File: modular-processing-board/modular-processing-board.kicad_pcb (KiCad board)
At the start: 6 copper layers, 90 x 90 mm, 175 parts, among them J1001 BWU.FL-IPEX1, J202 Conn_02x06_Odd_Even, J401 TF01A, J501 Plug_Hirose_DF40_2x40_DF40C-8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, J502 Conn_02x06_Odd_Even, J601 Conn_Coaxial_Small, J602 BWU.FL-IPEX1, J604 Conn_Coaxial_Small, J701 Conn_02x02_Odd_Even, J801 TYPE-C-31-M-12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

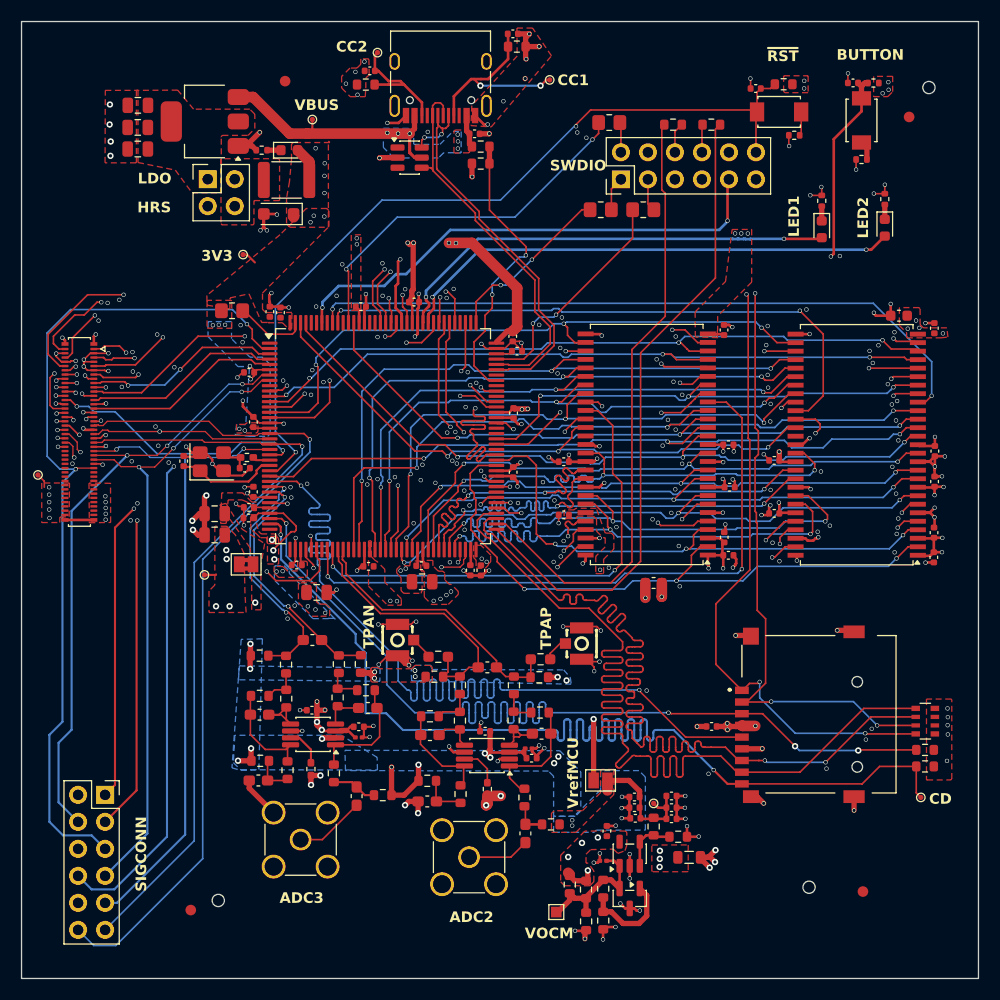
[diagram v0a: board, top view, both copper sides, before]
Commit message: checked components part numbers (next) board checks
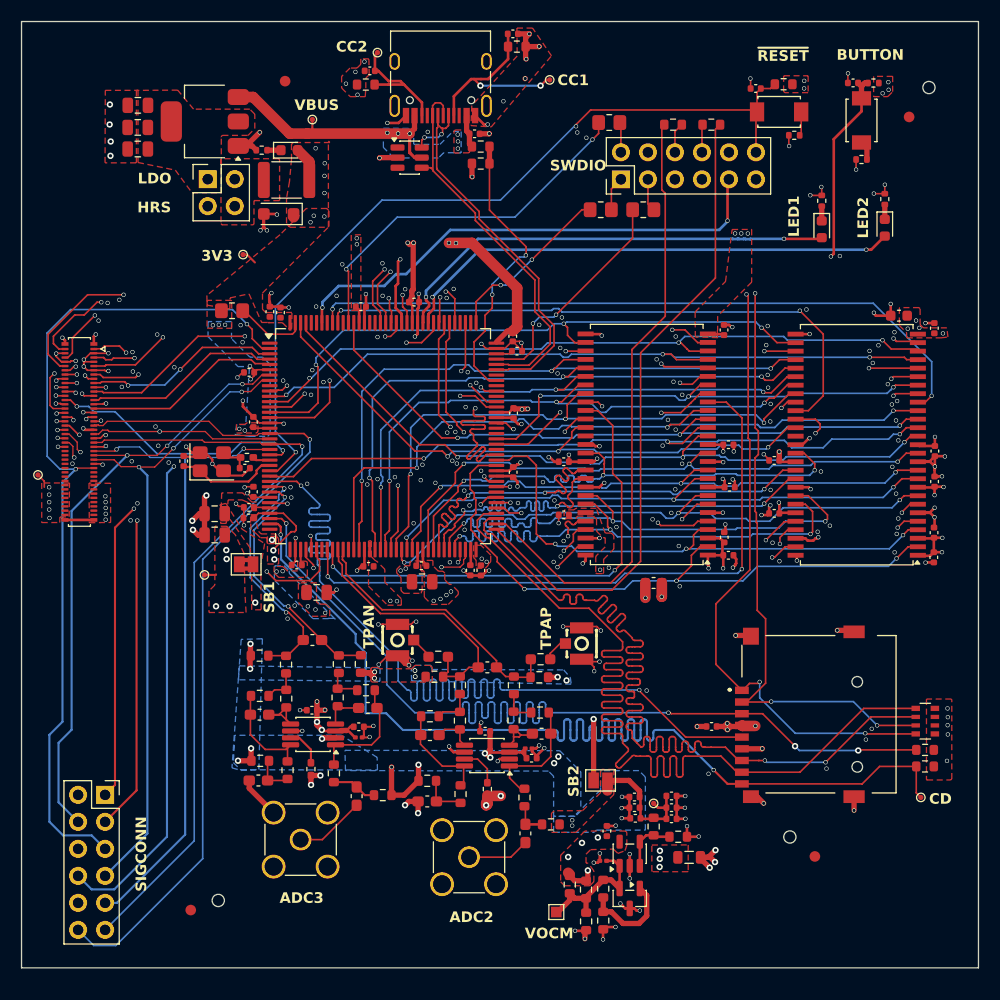
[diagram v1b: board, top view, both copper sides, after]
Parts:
- moved FID101 5.60 mm to (122.6, 126.5)
- moved H101 5.06 mm to (120.3, 124.7)
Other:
- board size 90 x 90 mm -> 90 x 89 mm
- board text added: "SB1"
- board text added: "SB2"
- board text added: "~{RESET}"
- board text removed: "VrefMCU"
- board text removed: "~{RST}"
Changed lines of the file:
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@@
 	(footprint "MountingHole:ToolingHole_1.152mm"
 		(layer "F.Cu")
-		(at 122.066 129.4178 90)
+		(at 120.2626 124.6934 90)
 		(descr "Tooling Hole 1.152mm, 1.3mm solder mask, JLCPCB specification, https://jlcpcb.com/help/article/How-to-add-tooling-holes-for-PCB-assembly-order")
 		(tags "mounting")
@@
 			(polygon
 				(pts
-					(xy 122.066 128.7178) (xy 121.898479 128.738141) (xy 121.740694 128.797981) (xy 121.601814 128.893842)
-					(xy 121.489911 129.020155) (xy 121.411489 129.169577) (xy 121.371104 129.333424) (xy 121.371104 129.502176)
-					(xy 121.411489 129.666023) (xy 121.489911 129.815445) (xy 121.601814 129.941758) (xy 121.740694 130.037619)
-					(xy 121.898479 130.097459) (xy 122.066 130.1178) (xy 122.233521 130.097459) (xy 122.391306 130.037619)
-					(xy 122.530186 129.941758) (xy 122.642089 129.815445) (xy 122.720511 129.666023) (xy 122.760896 129.502176)
-					(xy 122.760896 129.333424) (xy 122.720511 129.169577) (xy 122.642089 129.020155) (xy 122.530186 128.893842)
-					(xy 122.391306 128.797981) (xy 122.233521 128.738141)
+					(xy 120.2626 123.9934) (xy 120.095079 124.013741) (xy 119.937294 124.073581) (xy 119.798414 124.169442)
+					(xy 119.686511 124.295755) (xy 119.608089 124.445177) (xy 119.567704 124.609024) (xy 119.567704 124.777776)
+					(xy 119.608089 124.941623) (xy 119.686511 125.091045) (xy 119.798414 125.217358) (xy 119.937294 125.313219)
+					(xy 120.095079 125.373059) (xy 120.2626 125.3934) (xy 120.430121 125.373059) (xy 120.587906 125.313219)
+					(xy 120.726786 125.217358) (xy 120.838689 125.091045) (xy 120.917111 124.941623) (xy 120.957496 124.777776)
+					(xy 120.957496 124.609024) (xy 120.917111 124.445177) (xy 120.838689 124.295755) (xy 120.726786 124.169442)
+					(xy 120.587906 124.073581) (xy 120.430121 124.013741)
 				)
 			)
@@
 	(footprint "Fiducial:Fiducial_1mm_Mask2mm"
 		(layer "F.Cu")
-		(at 127.1354 129.826)
+		(at 122.6142 126.524)
 		(descr "Fiducial, circular marking, 1mm bare copper, 2mm soldermask opening (Level A)")
 		(tags "fiducial")
@@
 	(gr_rect
 		(start 48 48)
-		(end 138 138)
+		(end 138 137)
 		(stroke
 			(width 0.05)
@@
 		)
 	)
-	(gr_text "VrefMCU"
-		(at 100.457 122.047 90)
+	(gr_text "SB1"
+		(at 71.882 103.632 90)
+		(layer "F.SilkS")
+		(effects
+			(font
+				(size 1 1)
+				(thickness 0.2)
+				(bold yes)
+			)
+			(justify left bottom)
+		)
+	)
+	(gr_text "SB2"
+		(at 100.5078 120.9294 90)
 		(layer "F.SilkS")
 		(effects
@@
 		)
 	)
-	(gr_text "~{RST}"
-		(at 118.11 51.8414 0)
+	(gr_text "~{RESET}"
+		(at 117.1956 51.816 0)
 		(layer "F.SilkS")
 		(effects
@@
 		(polygon
 			(pts
-				(xy 58.801 54.473259) (xy 58.801 61.25815) (xy 58.76895 61.2902) (xy 55.8546 61.2902) (xy 55.8546 61.2902)
-				(xy 55.88 54.473259) (xy 58.9534 54.473259)
+				(xy 58.801 54.473259) (xy 58.801 61.25815) (xy 58.76895 61.2902) (xy 55.8546 61.2902) (xy 55.88 54.473259)
+				(xy 58.9534 54.473259)
 			)
 		)

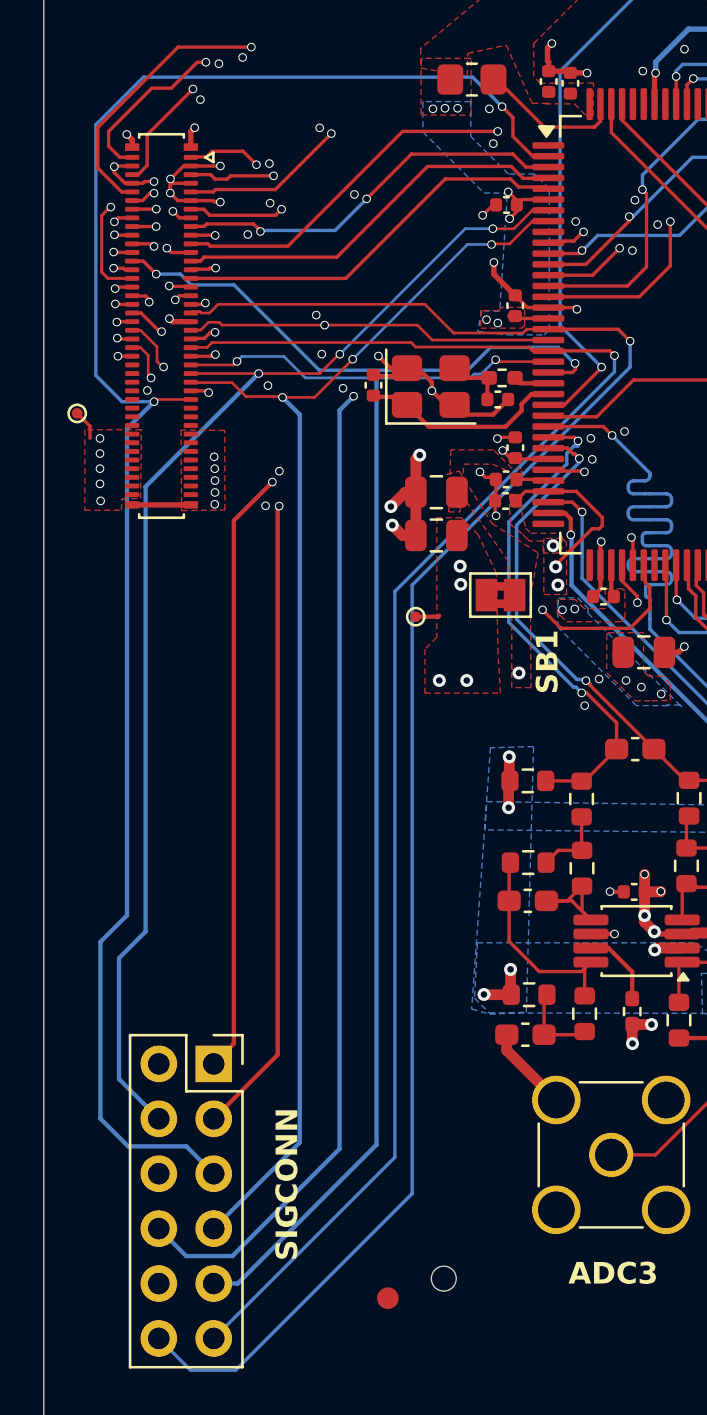
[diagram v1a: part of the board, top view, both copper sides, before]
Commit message: matched PSSI bus lenghts
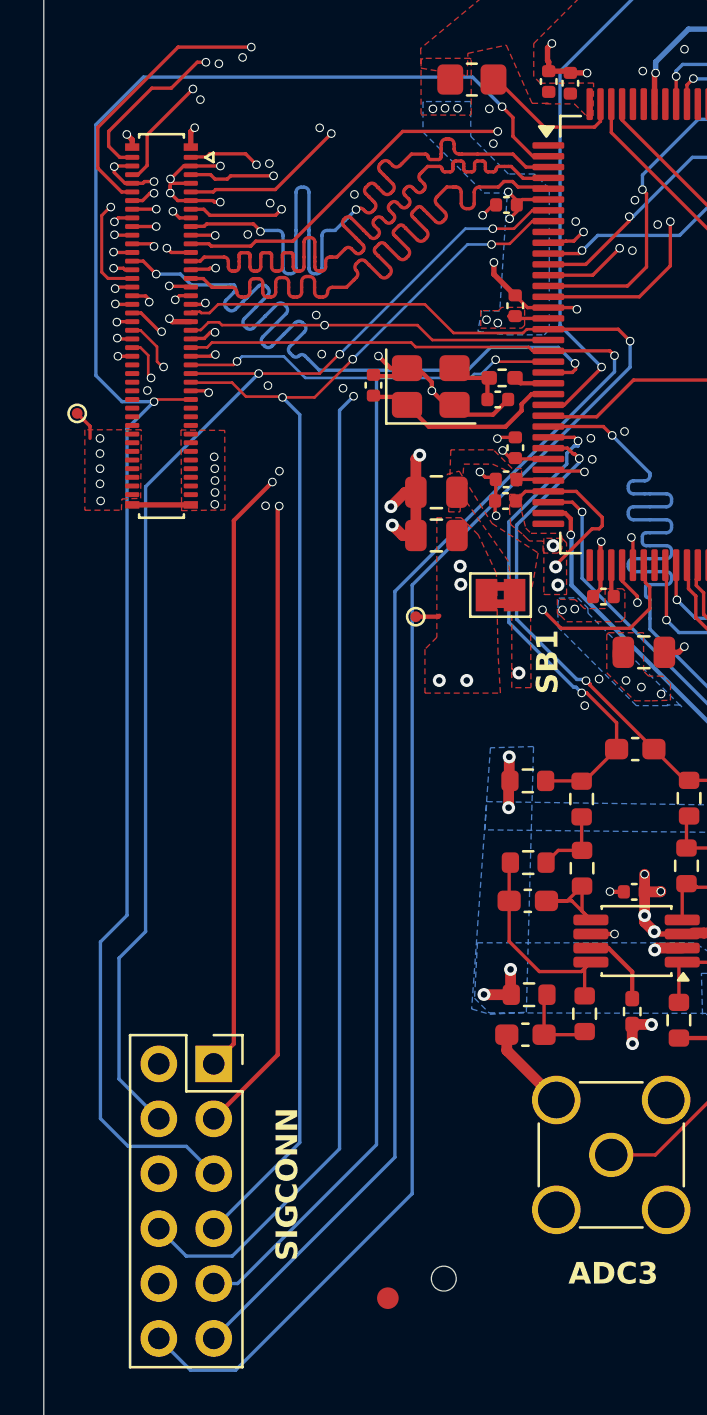
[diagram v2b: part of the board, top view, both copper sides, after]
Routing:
- net /connectors/PSSI.D6: track 18.6 -> 34.9 mm
- net /connectors/PSSI.D4: track 18.5 -> 34.5 mm
- net /connectors/PSSI.D7: track 18.6 -> 34.1 mm
- net /connectors/PSSI.D15: track 24.9 -> 36.0 mm
- net /connectors/PSSI.PDCK: track 32.5 -> 42.9 mm
- net /connectors/PSSI.D2: track 32.8 -> 40.3 mm
- net /connectors/PSSI.D14: track 31.0 -> 37.4 mm

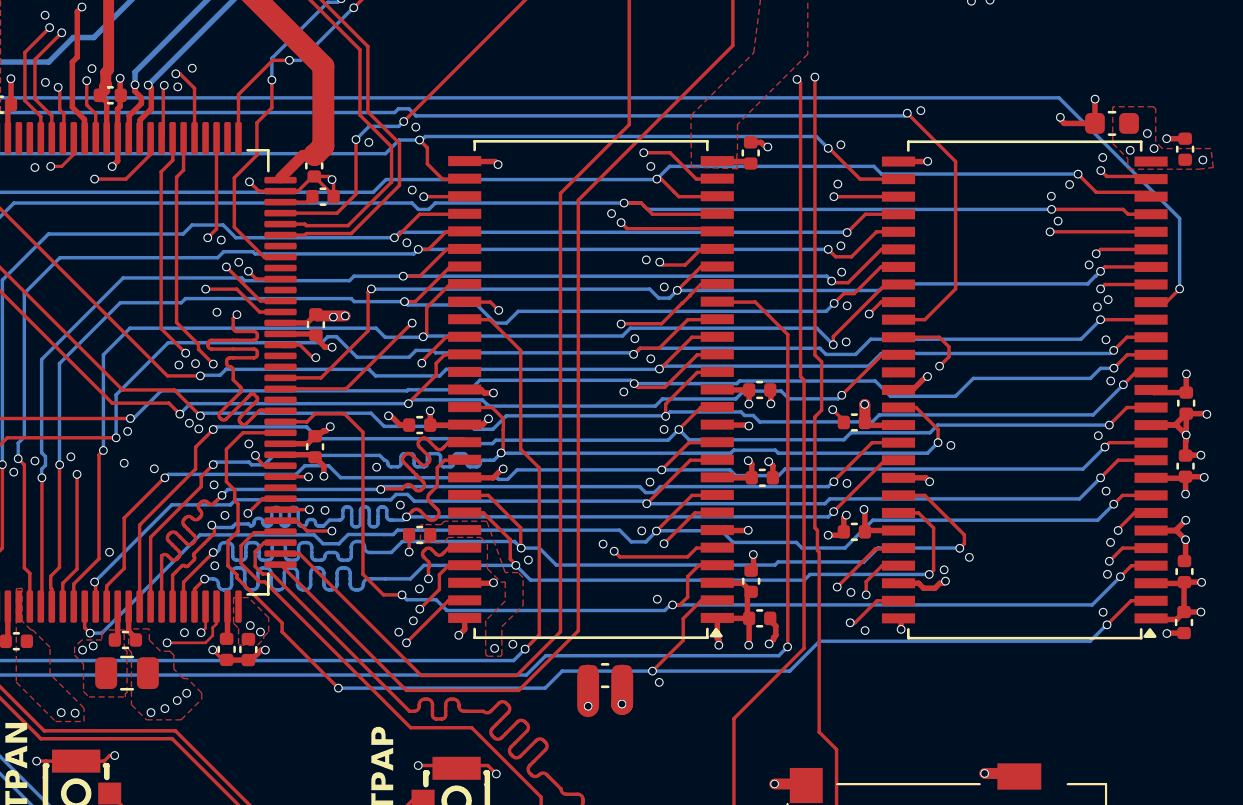
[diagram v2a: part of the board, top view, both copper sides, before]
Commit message: finished sdram length matching (next) check trace closeness for ADC-signals, check impedances, check SDMMC lengths
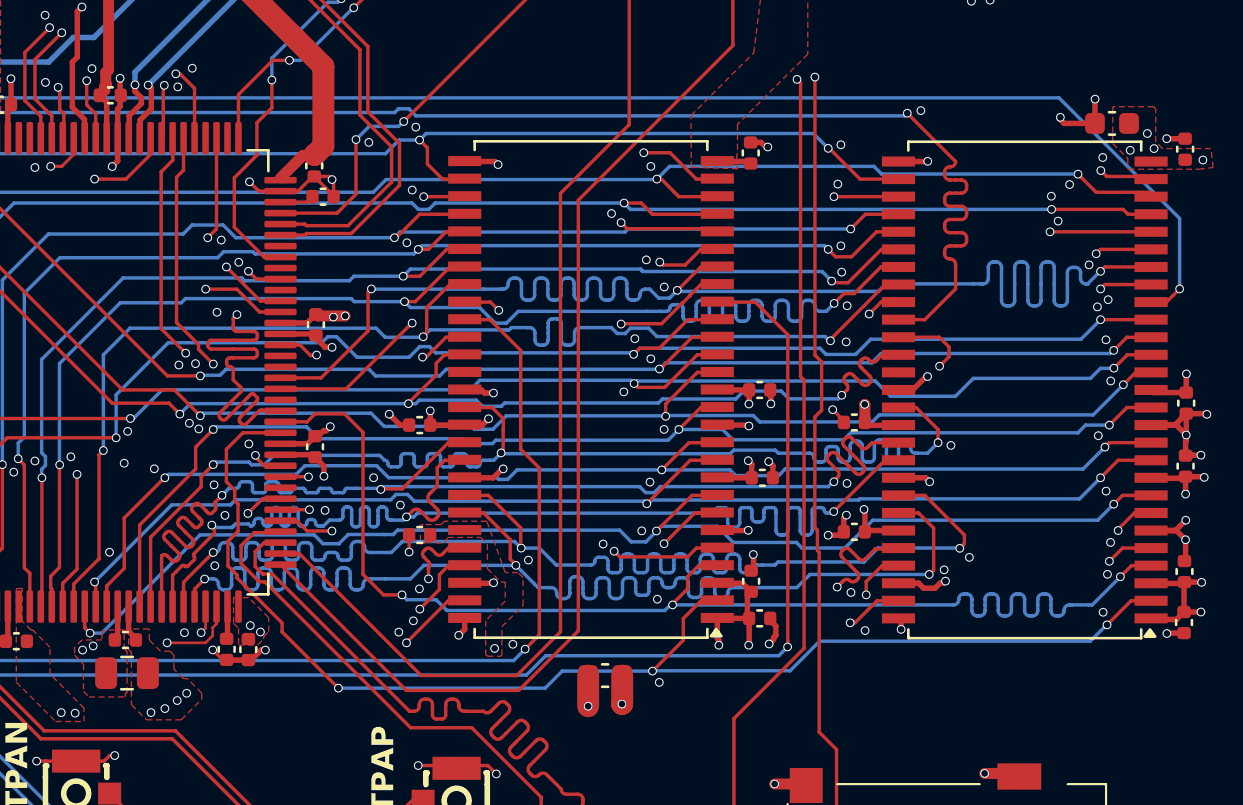
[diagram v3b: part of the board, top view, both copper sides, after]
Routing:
- net /mcu/SDRAM.CLK: track 37.7 -> 64.0 mm
- net /mcu/SDRAM.BS1: track 45.4 -> 64.6 mm
- net /mcu/SDRAM.BS0: track 47.1 -> 61.6 mm
- net /mcu/SDRAM.A12: track 51.4 -> 61.7 mm
- net /mcu/SDRAM.D13: track 54.0 -> 62.6 mm
- net /mcu/SDRAM.D12: track 51.3 -> 59.6 mm
- net /mcu/SDRAM.A9: track 55.6 -> 63.2 mm
- net /mcu/SDRAM.D11: track 52.4 -> 59.8 mm
- net /mcu/SDRAM.D10: track 50.6 -> 57.7 mm
- net /mcu/SDRAM.A5: track 55.4 -> 61.4 mm
- net /mcu/SDRAM.D1: track 51.4 -> 57.2 mm
- net /mcu/SDRAM.D8: track 51.0 -> 56.6 mm
- net /mcu/SDRAM.~{CKE1}: track 56.8 -> 62.0 mm
- net /mcu/SDRAM.D14: track 51.8 -> 56.5 mm
- net /mcu/SDRAM.D9: track 51.1 -> 55.4 mm
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
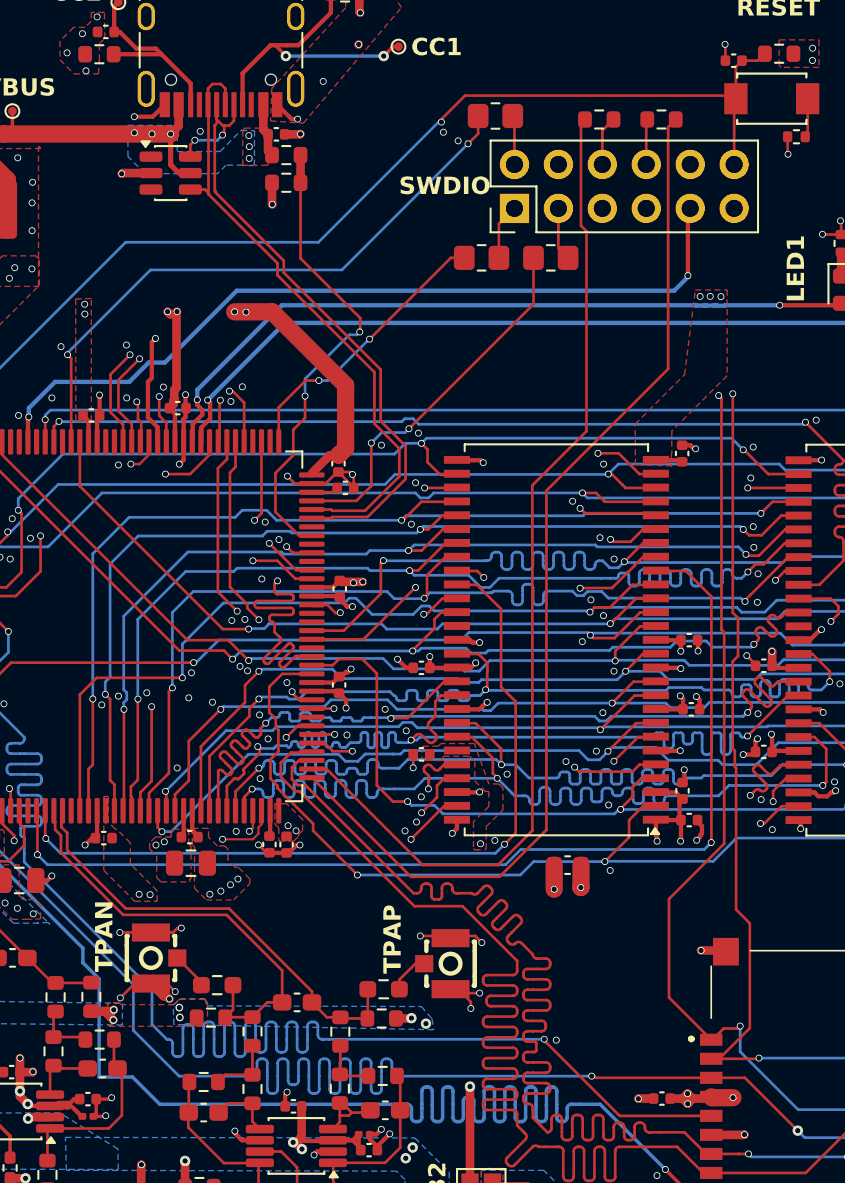
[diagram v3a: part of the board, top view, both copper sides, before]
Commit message: checked differential impedances + SDMMC lenghts (next) check impedances of SE-signals
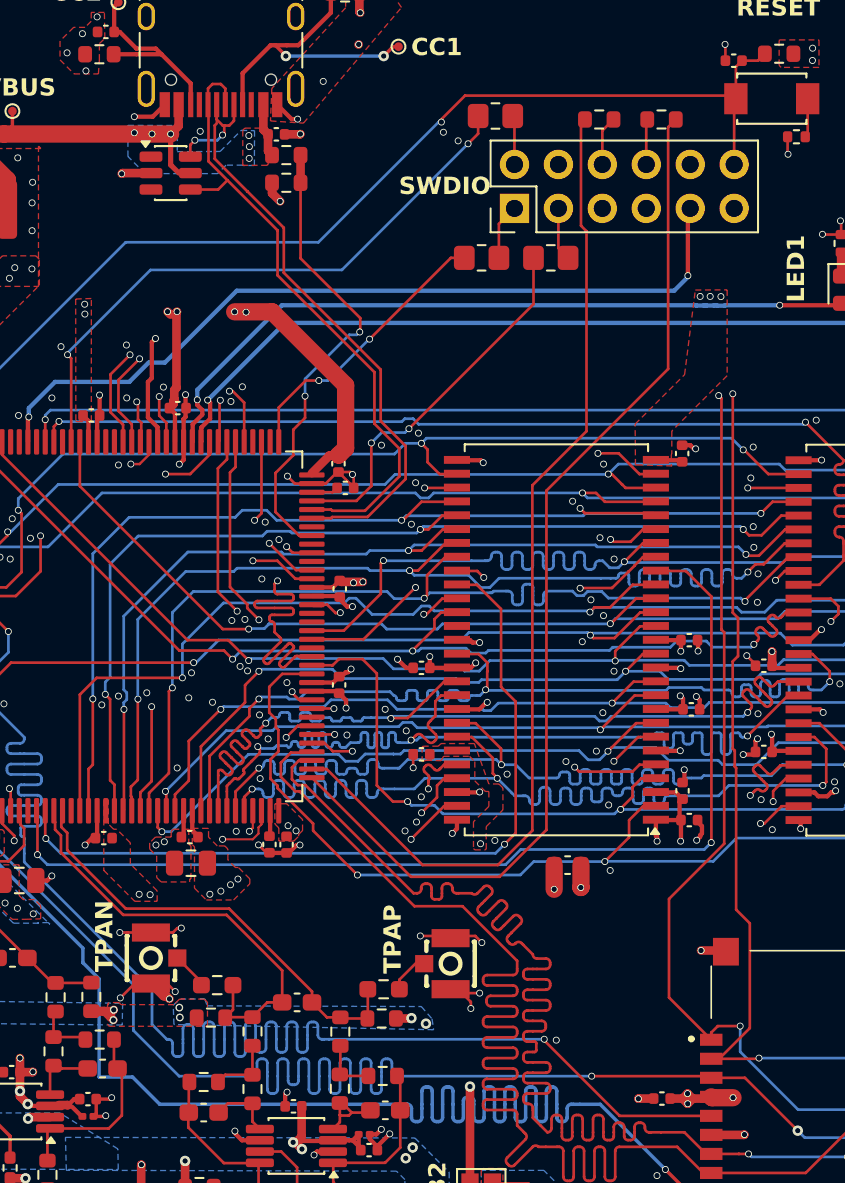
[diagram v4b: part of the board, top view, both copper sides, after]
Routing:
- net /mcu/USB_DP: track 36.3 -> 37.4 mm
